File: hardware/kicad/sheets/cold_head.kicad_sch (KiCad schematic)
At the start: 14 parts, among them J10 RTD PT1000 4-wire, U14 ADS1220IPW

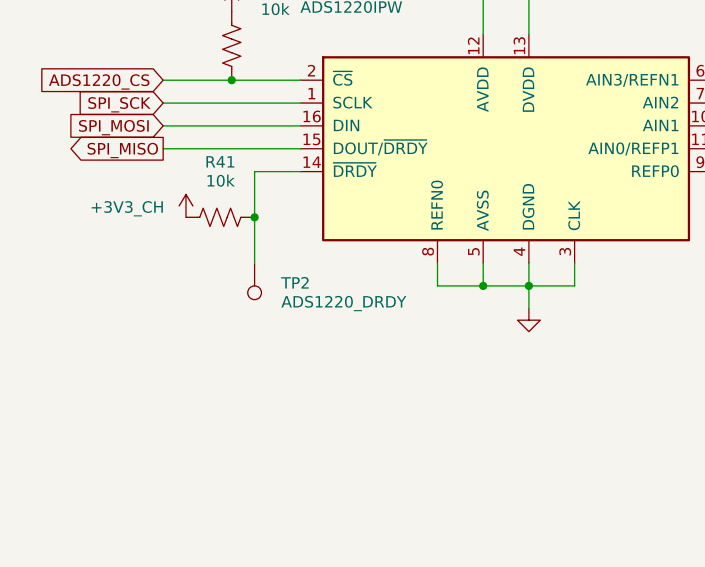
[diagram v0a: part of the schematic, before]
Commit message: WIP: restructure PCB for the Phoenix UCS 125-87 housing
Work in progress, layout not finished: about 90 parts still do not fit
their sections and the board is not routed.

- Right-angle connectors: Phoenix MSTBA 2,5 / MC 1,5, JST XH side entry,
  Hirose DF13, Molex 505448-0871 (new footprint from the Molex drawing)
- Datasheet and product links on every symbol (tools/part_links.py)
- Test points so every IC has one on its own nets
- gen_pcb.py: 100 x 62 mm two-sided board, housing holes and restricted
  corners, ESP32 antenna notch, one section per sheet, board ID block,
  ESP32 pin names, pin-1 marks, blue mask
- Housing drawings in hardware/housing/

Co-Authored-By: Claude Opus 5.5 <noreply@anthropic.com>
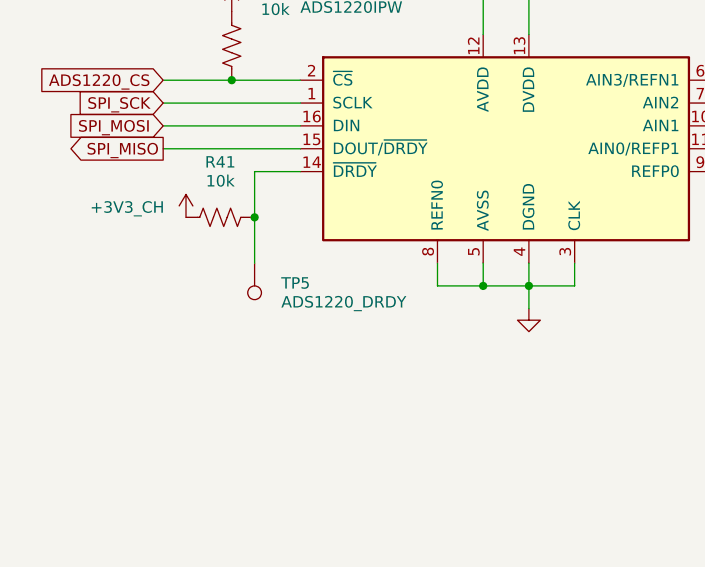
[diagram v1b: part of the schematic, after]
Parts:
- removed C31: 100nF, Capacitor_SMD:C_0603_1608Metric, symbol Device:C
- removed R41: 10k, Resistor_SMD:R_0603_1608Metric, symbol Device:R_US
- removed R42: 1k, Resistor_SMD:R_0603_1608Metric, symbol Device:R_US
- removed TP2: ADS1220_DRDY, TestPoint:TestPoint_Pad_D1.5mm, symbol Connector:TestPoint
- added C34: 100nF, Capacitor_SMD:C_0603_1608Metric, symbol Device:C
- added J10: RTD PT1000 4-wire, Connector_Hirose:Hirose_DF13-04P-1.25DS_1x04_P1.25mm_Horizontal, symbol Connector_Generic:Conn_01x04
- added R40: 10k, Resistor_SMD:R_0603_1608Metric, symbol Device:R_US
- added R44: 3.9k, Resistor_SMD:R_0603_1608Metric, symbol Device:R_US
- C31: renamed from R40; value 10k -> 100nF; footprint Resistor_SMD:R_0603_1608Metric -> Capacitor_SMD:C_0603_1608Metric; symbol Device:R_US -> Device:C; Product (none) -> https://www.digikey.com/en/products/result?keywords=C0603C1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
- C32: Product (none) -> https://www.digikey.com/en/products/result?keywords=08055C1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
- C33: renamed from R43; value 1k -> 10nF; footprint Resistor_SMD:R_0603_1608Metric -> Capacitor_SMD:C_0603_1608Metric; symbol Device:R_US -> Device:C; Product (none) -> https://www.digikey.com/en/products/result?keywords=CL10B10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
- C35: Product (none) -> https://www.digikey.com/en/products/result?keywords=CL10B10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
- C36: Product (none) -> https://www.digikey.com/en/products/result?keywords=C0603C1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
- R41: renamed from J10; value RTD PT1000 4-wire -> 10k; footprint Connector_JST:JST_XH_B4B-XH-A_1x04_P2.50mm_Vertical -> Resistor_SMD:R_0603_1608Metric; symbol Connector_Generic:Conn_01x04 -> Device:R_US; Product (none) -> https://www.digikey.com/en/products/result?keywords=AR0603F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
- R42: renamed from C34; value 100nF -> 1k; footprint Capacitor_SMD:C_0603_1608Metric -> Resistor_SMD:R_0603_1608Metric; symbol Device:C -> Device:R_US; Product (none) -> https://www.digikey.com/en/products/result?keywords=RC0603F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
- R43: renamed from R44; value 3.9k -> 1k; Product (none) -> https://www.digikey.com/en/products/result?keywords=RC0603F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
- TP5: renamed from C33; value 10nF -> ADS1220_DRDY; footprint Capacitor_SMD:C_0603_1608Metric -> TestPoint:TestPoint_Pad_D1.5mm; symbol Device:C -> Connector:TestPoint
- U14: Product (none) -> https://www.digikey.com/en/products/result?keywords=ADS1220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
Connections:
- net +3V3: now also R40.1; no longer C31.1
- net +3V3_CH: now also C31.1, R41.1
- net ADS1220_CS: now also R40.2; no longer C31.2
- net GND: now also C31.2, C33.2, R44.2; no longer R43.2, TP5.2
- net at R42.1, U14.10 (AIN1): now also C33.1, C34.1; no longer TP5.1
- net at C35.1, U14.11 (AIN0/REFP1): now also R43.1, C34.2; no longer C33.1, R42.2
- net at R41.2: now also TP5.1, U14.14 (~{DRDY})
- net at U14.6 (AIN3/REFN1): now also J10.1 (Pin_1); no longer R41.1 (Pin_1)
- net at C36.1, U14.9 (REFP0): now also J10.4 (Pin_4), R44.1; no longer R41.4 (Pin_4), R43.1
- new net: J10.2 (Pin_2), R42.2
- new net: J10.3 (Pin_3), R43.2
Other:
- moved on the sheet: R43

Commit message: Lay out the board for the Phoenix UCS 145-125 housing
Move to a 120 x 100 mm, 4-layer, blue-mask board for the UCS 145-125-F-CCD
7035 housing: housing mounting holes and restricted corners, ESP32 antenna
over a routed notch, one labelled section per schematic sheet with almost
every part on top. Placed, routed and cleaned up: DRC 0 errors, 0
unconnected, 0 schematic-parity issues; ERC 0; 193/193 datasheet rules.

- AGENTS.md: test points go on the same side as the part they test, close
  to it
- gen_pcb: test points held to their IC's side and within 8 mm; silkscreen
  check measures text by ink and also fails on pads, part outlines, section
  lines and pin-1 dots; titles along or up a border; connector labels and
  ESP32 pin names reserved before the passives; pin-1 dots only where the
  footprint has no mark; footprints carry the schematic's library links and
  fields; mounting holes are board-only H1-H4
- fix_route: generic clean-up (no old-board coordinate edits); removes GND
  vias in keep-outs or on foreign pads, links stranded ground pads, nudges
  squeezed tracks, handles back-side pour islands
- kicad_dru: fix the rule file (an invalid USB-C rule made KiCad ignore it);
  housing-corner and antenna keep-out part rules
- schematic: pad test points excluded from the BOM
- README / fabrication README updated for the new board

Co-Authored-By: Claude Opus 5.5 <noreply@anthropic.com>
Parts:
- TP5: now left out of the parts list
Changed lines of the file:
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@@
 		(body_style 1)
 		(exclude_from_sim no)
-		(in_bom yes)
+		(in_bom no)
 		(on_board yes)
 		(in_pos_files yes)

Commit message: Use an M12 receptacle for the PT1000 and JST PH headers for the 2-pin I/O
- J10 (cold head PT1000): TE T4145035041-001, M12 A-coded 4-pin female,
  right angle, shielded, panel and PCB mount through the right side wall;
  footprint from TE drawing T41450350X1001 rev B
- J6, J7, J13 (NTC, panel button, relay out): Adafruit 1769 (4UCON 17311),
  JST PH compatible 2-pin right-angle SMT; footprint from its drawing
- BOM, part links and 3D envelopes for both; schematic nets unchanged
- gen_pcb: ground fan-out before routing (a locked via and short track per
  small ground pad, clear of other holes) so no ground pad is left on a
  pour island; fallback labels must sit inside a section box
- fix_route: skip paste apertures (not non-plated holes) as foreign copper,
  nudge tracks off crowded pads, remove GND vias that crowd another hole

DRC 0 errors, 0 unconnected, 0 schematic-parity issues; ERC 0; 193/193
datasheet rules.

Co-Authored-By: Claude Opus 5.5 <noreply@anthropic.com>
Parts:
- J10: footprint Connector_Hirose:Hirose_DF13-04P-1.25DS_1x04_P1.25mm_Horizontal -> cryocooler:TE_T4145035041-001_M12_A-Code_4P_Female_Horizontal; Product https://www.digikey.com/en/products/result?keywords=DF13-4P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 -> https://www.te.com/en/product-T4145035041-001.html
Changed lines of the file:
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@@
 			)
 		)
-		(property "Footprint" "Connector_Hirose:Hirose_DF13-04P-1.25DS_1x04_P1.25mm_Horizontal"
+		(property "Footprint" "cryocooler:TE_T4145035041-001_M12_A-Code_4P_Female_Horizontal"
 			(at 215.9 76.2 0)
 			(hide yes)
@@
 			)
 		)
-		(property "Datasheet" "https://www.hirose.com/api/v1/series/DF13/documents/product_series_catalog/content?lang=EN"
+		(property "Datasheet" "https://www.te.com/commerce/DocumentDelivery/DDEController?Action=srchrtrv&DocNm=T41450350X1001&DocType=Customer%20Drawing&DocLang=English&DocFormat=pdf&PartCntxt=T4145035041-001"
 			(at 215.9 76.2 0)
 			(hide yes)
@@
 			)
 		)
-		(property "Product" "https://www.digikey.com/en/products/result?keywords=DF13-4P-1.25DS%2825%29"
+		(property "Product" "https://www.te.com/en/product-T4145035041-001.html"
 			(at 215.9 76.2 0)
 			(hide yes)

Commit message: Ground the M12 shield, order the ground loops, name the J14 cable parts
- J10: shielded symbol (Conn_01x04_Shielded); the M12 shield pin and its
  four shell legs are pad SH, tied to GND
- TP22-TP25: Keystone 5001 black miniature PC test points (KiCad
  TestPoint_Keystone_5000-5004 footprint, 1.02 mm hole per Keystone's
  drawing); now in the BOM, the bare pad test points stay out
- J14 BOM note: cable housing Molex 5054320801 with 505431 terminals, or
  tin pre-crimped leads 797581148 / 797581149 (from molex.com)

Only netlist change: GND gains J10 SH. DRC 0 errors, 0 unconnected, 0
schematic-parity issues; ERC 0; 193/193 datasheet rules.

Co-Authored-By: Claude Opus 5.5 <noreply@anthropic.com>
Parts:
- removed C34: 100nF, Capacitor_SMD:C_0603_1608Metric, symbol Device:C
- removed R42: 1k, Resistor_SMD:R_0603_1608Metric, symbol Device:R_US
- added C33, C35: 10nF, Capacitor_SMD:C_0603_1608Metric, symbol Device:C
- C34: renamed from R43; value 1k -> 100nF; footprint Resistor_SMD:R_0603_1608Metric -> Capacitor_SMD:C_0603_1608Metric; symbol Device:R_US -> Device:C; Product https://www.digikey.com/en/products/result?keywords=RC0603F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 -> https://www.digikey.com/en/products/result?keywords=C0603C1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
- J10: symbol Connector_Generic:Conn_01x04 -> Connector_Generic_Shielded:Conn_01x04_Shielded
- R42: renamed from C33; value 10nF -> 1k; footprint Capacitor_SMD:C_0603_1608Metric -> Resistor_SMD:R_0603_1608Metric; symbol Device:C -> Device:R_US; Product https://www.digikey.com/en/products/result?keywords=CL10B10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 -> https://www.digikey.com/en/products/result?keywords=RC0603F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
- R43: renamed from C35; value 10nF -> 1k; footprint Capacitor_SMD:C_0603_1608Metric -> Resistor_SMD:R_0603_1608Metric; symbol Device:C -> Device:R_US; Product https://www.digikey.com/en/products/result?keywords=CL10B10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 -> https://www.digikey.com/en/products/result?keywords=RC0603F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
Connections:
- net GND: now also J10.SH (Shield), C33.2, C35.2; no longer R42.2, R43.2
- net at R42.1, U14.10 (AIN1): now also C34.1, C33.1
- net at J10.2 (Pin_2): now also R42.2
- net at R43.1, U14.11 (AIN0/REFP1): now also C34.2, C35.1; no longer C34.1
- net at J10.3 (Pin_3): now also R43.2; no longer C34.2
